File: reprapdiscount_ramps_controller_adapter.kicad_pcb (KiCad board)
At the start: 2 copper layers, 62.1 x 21.2 mm, 0 parts

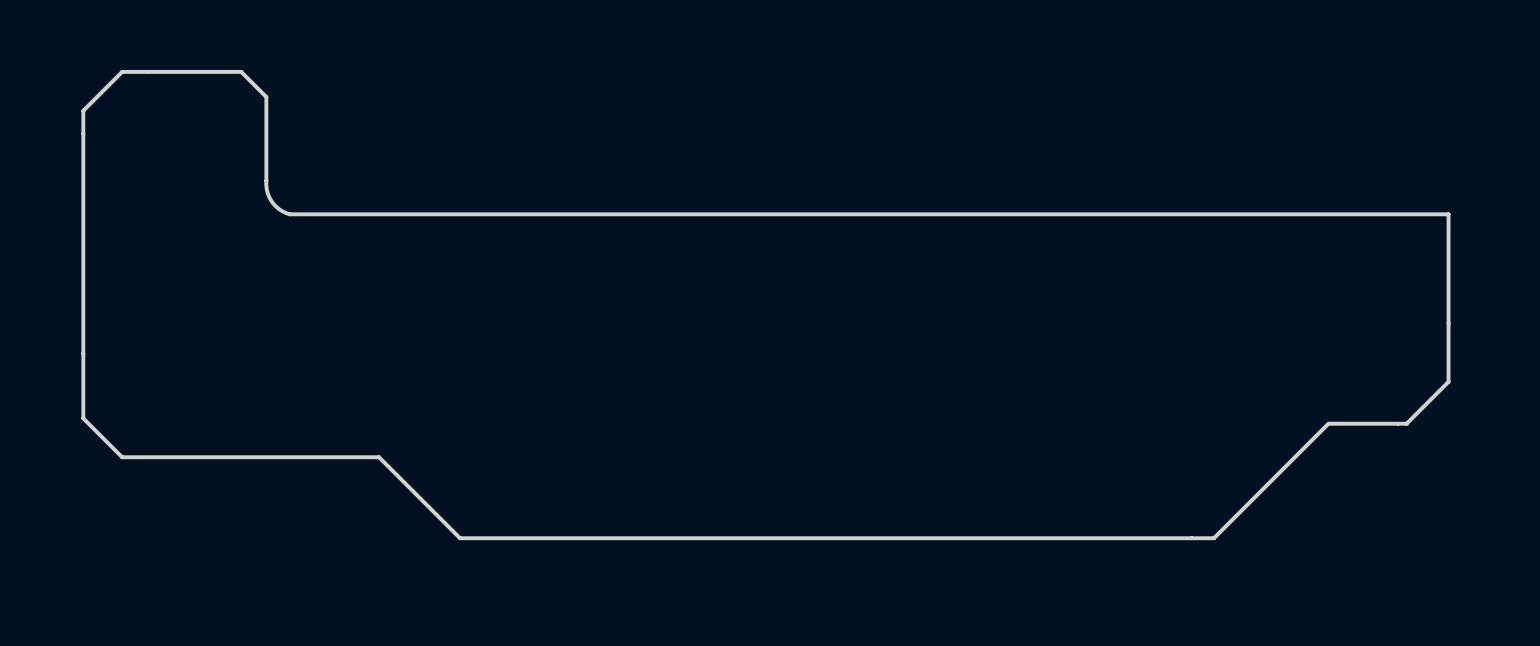
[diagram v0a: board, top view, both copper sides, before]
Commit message: adapter: finish routing
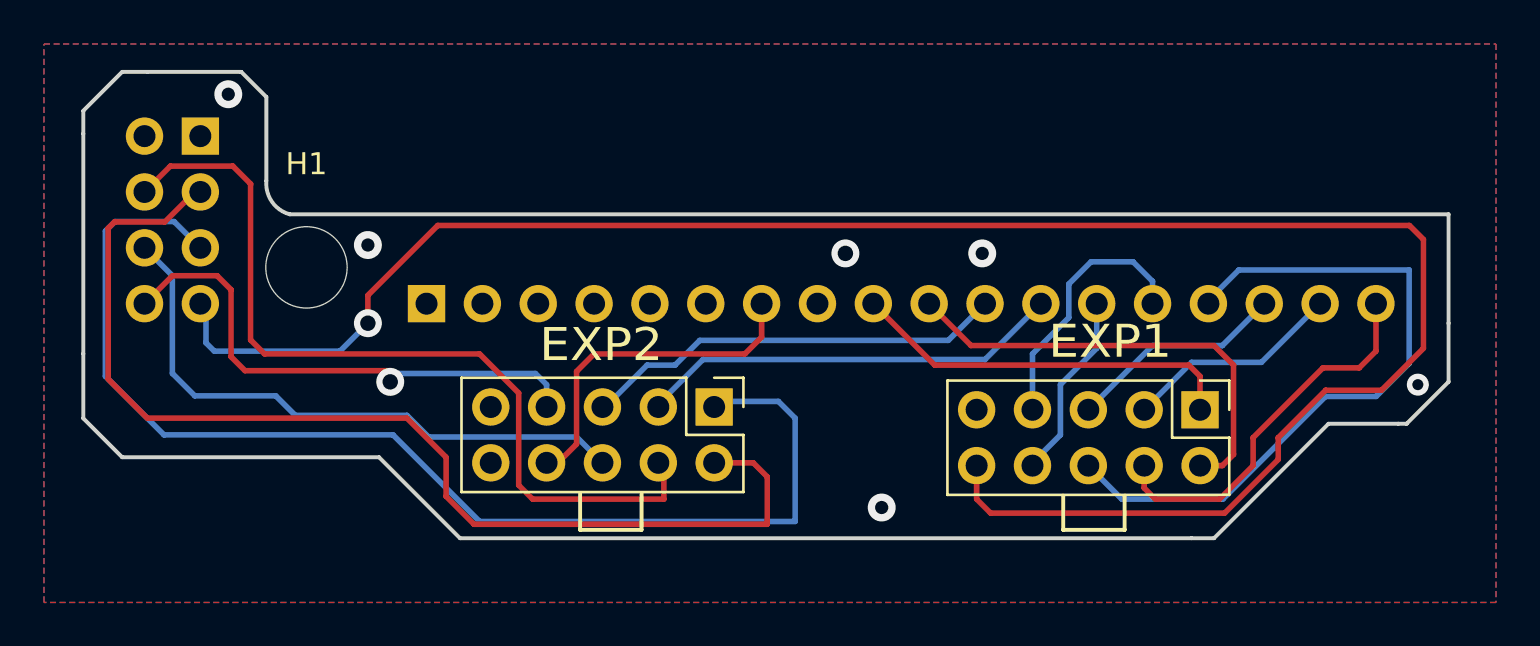
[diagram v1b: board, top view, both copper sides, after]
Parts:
- added AUX-3: Conn_02x04_Odd_Even, Gigahawk:PinSocket_2x04_P2.54mm_Vertical_Flipped, B.Cu at (71.9, -70.7)
- added AUX-4: Conn_01x18, Connector_PinSocket_2.54mm:PinSocket_1x18_P2.54mm_Vertical, B.Cu at (84.7, -63.1)
- added EXP1: Header 5X2, Connector_PinHeader_2.54mm:PinHeader_2x05_P2.54mm_Vertical, F.Cu at (119.9, -58.3)
- added EXP2: Header 5X2, Connector_PinHeader_2.54mm:PinHeader_2x05_P2.54mm_Vertical, F.Cu at (97.8, -58.4)
- added H1: MountingHole, MountingHole:MountingHole_3.7mm, F.Cu at (79.2, -64.8)
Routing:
- net A10: track 0.00 -> 91.5 mm, vias 0 -> 1
- net B1: track 0.00 -> 54.5 mm
- net B2: track 0.00 -> 50.3 mm
- net B4: track 0.00 -> 38.8 mm
- net A6: track 0.00 -> 31.9 mm
- net B6: track 0.00 -> 27.5 mm
- net B7: track 0.00 -> 24.3 mm, vias 0 -> 1
- net A2: track 0.00 -> 20.8 mm
- net B3: track 0.00 -> 19.4 mm
- net B5: track 0.00 -> 19.3 mm
- net A1: track 0.00 -> 17.8 mm
- net A4: track 0.00 -> 17.5 mm
- net B8: track 0.00 -> 15.6 mm
- net A7: track 0.00 -> 12.0 mm
- net A5: track 0.00 -> 10.00 mm
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- added copper zone on B.Cu, net GND
- added copper zone on F.Cu, net GND

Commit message: adapter: update silkscreen
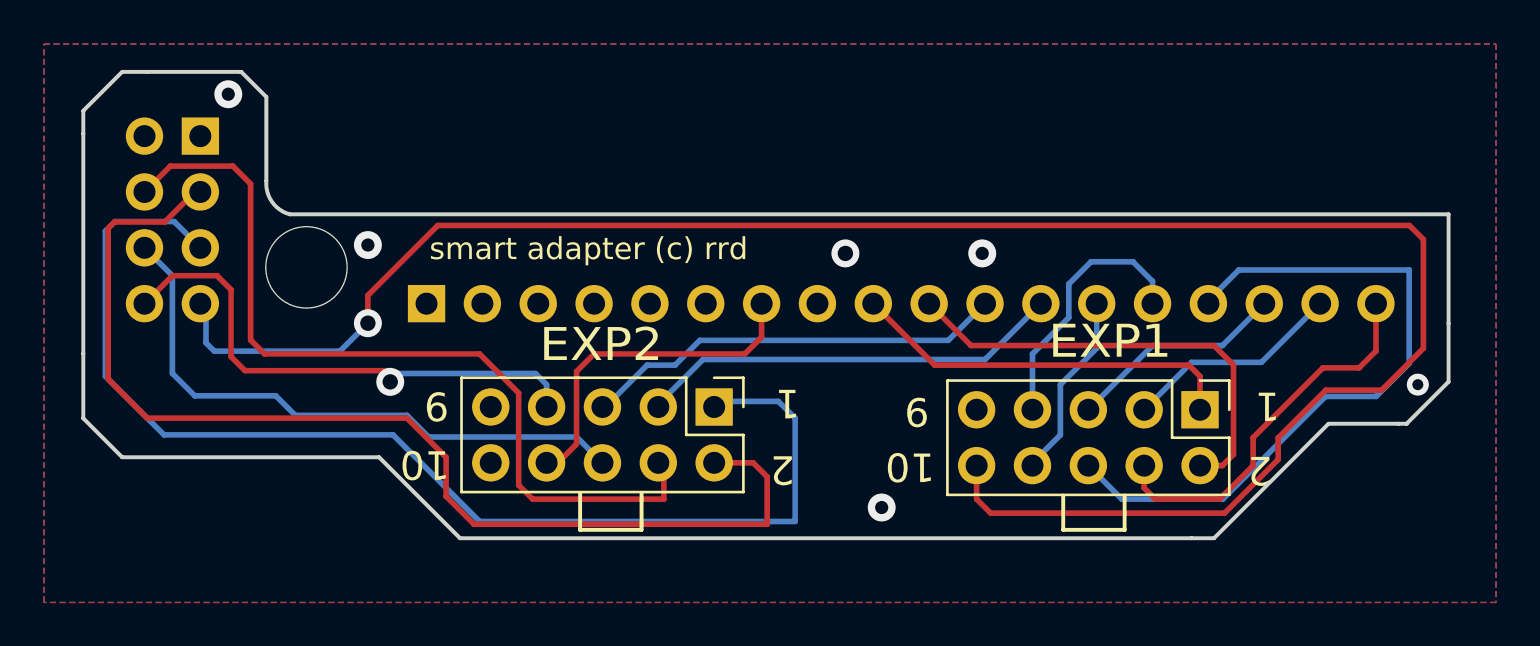
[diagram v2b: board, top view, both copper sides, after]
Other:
- board text added: "1"
- board text added: "10"
- board text added: "2"
- board text added: "9"
- board text added: "smart adapter (c) rrd"
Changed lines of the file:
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@@
     (property "ki_keywords" "mounting hole")
     (attr exclude_from_pos_files)
-    (fp_text reference "H1" (at 0 -4.7) (layer "F.SilkS")
+    (fp_text reference "H1" (at 0 -4.7) (layer "F.SilkS") hide
         (effects (font (size 1 1) (thickness 0.15)))
     )
@@
     (property "ki_keywords" "connector")
     (attr through_hole)
-    (fp_text reference "AUX-3" (at -1.27 2.77) (layer "B.SilkS")
-        (effects (font (size 1 1) (thickness 0.15)) (justify mirror))
+    (fp_text reference "AUX-3" (at -4.5212 -3.2258 270 unlocked) (layer "B.SilkS")
+        (effects (font (size 1.5 1.5) (thickness 0.254) bold) (justify mirror))
     )
     (fp_text value "Conn_02x04_Odd_Even" (at -1.27 -10.39) (layer "B.Fab")
@@
     (property "ki_keywords" "connector")
     (attr through_hole)
-    (fp_text reference "AUX-4" (at 0 2.77 90) (layer "B.SilkS")
-        (effects (font (size 1 1) (thickness 0.15)) (justify mirror))
+    (fp_text reference "AUX-4" (at -2.4638 -38.7858 -180) (layer "B.SilkS")
+        (effects (font (size 1.5 1.5) (thickness 0.254) bold) (justify mirror))
     )
     (fp_text value "Conn_01x18" (at 0 -45.95 90) (layer "B.Fab")
@@
   (gr_line (start 119.507 -52.451) (end 120.523 -52.451)
     (stroke (width 0.1778) (type solid)) (layer "Edge.Cuts"))
+  (gr_text "2" (at 71.8058 -61.1632 90) (layer "B.SilkS")
+    (effects (font (size 1.3 1.3) (thickness 0.2)) (justify mirror))
+  )
+  (gr_text "1" (at 74.3458 -61.214 90) (layer "B.SilkS")
+    (effects (font (size 1.3 1.3) (thickness 0.2)) (justify mirror))
+  )
+  (gr_text "2" (at 100.8888 -55.5752 180) (layer "F.SilkS")
+    (effects (font (size 1.3 1.3) (thickness 0.2)))
+  )
+  (gr_text "1" (at 101.1428 -58.5978 180) (layer "F.SilkS")
+    (effects (font (size 1.3 1.3) (thickness 0.2)))
+  )
+  (gr_text "smart adapter (c) rrd" (at 84.836 -65.024) (layer "F.SilkS")
+    (effects (font (size 1 1) (thickness 0.15)) (justify left bottom))
+  )
+  (gr_text "9" (at 85.1662 -58.4708 180) (layer "F.SilkS")
+    (effects (font (size 1.3 1.3) (thickness 0.2)))
+  )
+  (gr_text "10" (at 84.6328 -55.8038 180) (layer "F.SilkS")
+    (effects (font (size 1.3 1.3) (thickness 0.2)))
+  )
+  (gr_text "2" (at 122.6058 -55.5498 180) (layer "F.SilkS")
+    (effects (font (size 1.3 1.3) (thickness 0.2)))
+  )
+  (gr_text "9" (at 107.0102 -58.2168 180) (layer "F.SilkS")
+    (effects (font (size 1.3 1.3) (thickness 0.2)))
+  )
+  (gr_text "1" (at 122.9614 -58.4708 180) (layer "F.SilkS")
+    (effects (font (size 1.3 1.3) (thickness 0.2)))
+  )
+  (gr_text "10" (at 106.7054 -55.7022 180) (layer "F.SilkS")
+    (effects (font (size 1.3 1.3) (thickness 0.2)))
+  )
   (via (at 129.794 -59.436) (size 1) (drill 0.5) (layers "F.Cu" "B.Cu") (net 0))
   (segment (start 85.598 -56.134) (end 83.82 -57.912) (width 0.254) (layer "F.Cu") (net 2))

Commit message: adapter: clean up schematic
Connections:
- net A1 renamed BEEPER
- net A10 renamed VCC
- net A2 renamed BTN_ENC
- net A3 renamed LCDE
- net A4 renamed LCDRS
- net A5 renamed LCD4
- net A6 renamed LCD5
- net A7 renamed LCD6
- net A8 renamed LCD7
- net B1 renamed SD_MISO
- net B2 renamed HOST_SCK
- net B3 renamed BTN_EN2
- net B4 renamed HOST_CS
- net B5 renamed BTN_EN1
- net B6 renamed HOST_MOSI
- net B7 renamed SD_DET
- net B8 renamed RESET
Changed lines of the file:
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@@
   (net 0 "")
   (net 1 "unconnected-(AUX-3-Pin_2-Pad2)")
-  (net 2 "B2")
-  (net 3 "B4")
-  (net 4 "B1")
-  (net 5 "B6")
-  (net 6 "A10")
-  (net 7 "B7")
+  (net 2 "HOST_SCK")
+  (net 3 "HOST_CS")
+  (net 4 "SD_MISO")
+  (net 5 "HOST_MOSI")
+  (net 6 "VCC")
+  (net 7 "SD_DET")
   (net 8 "unconnected-(AUX-4-Pin_1-Pad1)")
   (net 9 "unconnected-(AUX-4-Pin_2-Pad2)")
@@
   (net 12 "unconnected-(AUX-4-Pin_5-Pad5)")
   (net 13 "unconnected-(AUX-4-Pin_6-Pad6)")
-  (net 14 "B8")
+  (net 14 "RESET")
   (net 15 "unconnected-(AUX-4-Pin_8-Pad8)")
-  (net 16 "A1")
-  (net 17 "A2")
-  (net 18 "B5")
-  (net 19 "B3")
-  (net 20 "A8")
-  (net 21 "A7")
-  (net 22 "A6")
-  (net 23 "A5")
-  (net 24 "A3")
-  (net 25 "A4")
+  (net 16 "BEEPER")
+  (net 17 "BTN_ENC")
+  (net 18 "BTN_EN1")
+  (net 19 "BTN_EN2")
+  (net 20 "LCD7")
+  (net 21 "LCD6")
+  (net 22 "LCD5")
+  (net 23 "LCD4")
+  (net 24 "LCDE")
+  (net 25 "LCDRS")
   (net 26 "B9")
   (net 27 "B10")
@@
       (stroke (width 0.1) (type solid)) (layer "F.Fab"))
     (pad "1" thru_hole rect (at 0 0 270) (size 1.7 1.7) (drill 1) (layers "*.Cu" "*.Mask")
-      (net 4 "B1") (pinfunction "1") (pintype "passive"))
+      (net 4 "SD_MISO") (pinfunction "1") (pintype "passive"))
     (pad "2" thru_hole oval (at 2.54 0 270) (size 1.7 1.7) (drill 1) (layers "*.Cu" "*.Mask")
-      (net 2 "B2") (pinfunction "2") (pintype "passive"))
+      (net 2 "HOST_SCK") (pinfunction "2") (pintype "passive"))
     (pad "3" thru_hole oval (at 0 2.54 270) (size 1.7 1.7) (drill 1) (layers "*.Cu" "*.Mask")
-      (net 19 "B3") (pinfunction "3") (pintype "passive"))
+      (net 19 "BTN_EN2") (pinfunction "3") (pintype "passive"))
     (pad "4" thru_hole oval (at 2.54 2.54 270) (size 1.7 1.7) (drill 1) (layers "*.Cu" "*.Mask")
-      (net 3 "B4") (pinfunction "4") (pintype "passive"))
+      (net 3 "HOST_CS") (pinfunction "4") (pintype "passive"))
     (pad "5" thru_hole oval (at 0 5.08 270) (size 1.7 1.7) (drill 1) (layers "*.Cu" "*.Mask")
-      (net 18 "B5") (pinfunction "5") (pintype "passive"))
+      (net 18 "BTN_EN1") (pinfunction "5") (pintype "passive"))
     (pad "6" thru_hole oval (at 2.54 5.08 270) (size 1.7 1.7) (drill 1) (layers "*.Cu" "*.Mask")
-      (net 5 "B6") (pinfunction "6") (pintype "passive"))
+      (net 5 "HOST_MOSI") (pinfunction "6") (pintype "passive"))
     (pad "7" thru_hole oval (at 0 7.62 270) (size 1.7 1.7) (drill 1) (layers "*.Cu" "*.Mask")
-      (net 7 "B7") (pinfunction "7") (pintype "passive"))
+      (net 7 "SD_DET") (pinfunction "7") (pintype "passive"))
     (pad "8" thru_hole oval (at 2.54 7.62 270) (size 1.7 1.7) (drill 1) (layers "*.Cu" "*.Mask")
-      (net 14 "B8") (pinfunction "8") (pintype "passive"))
+      (net 14 "RESET") (pinfunction "8") (pintype "passive"))
     (pad "9" thru_hole oval (at 0 10.16 270) (size 1.7 1.7) (drill 1) (layers "*.Cu" "*.Mask")
       (net 26 "B9") (pinfunction "9") (pintype "passive"))
@@
       (stroke (width 0.1) (type solid)) (layer "F.Fab"))
     (pad "1" thru_hole rect (at 0 0 270) (size 1.7 1.7) (drill 1) (layers "*.Cu" "*.Mask")
-      (net 16 "A1") (pinfunction "1") (pintype "passive"))
+      (net 16 "BEEPER") (pinfunction "1") (pintype "passive"))
     (pad "2" thru_hole oval (at 2.54 0 270) (size 1.7 1.7) (drill 1) (layers "*.Cu" "*.Mask")
-      (net 17 "A2") (pinfunction "2") (pintype "passive"))
+      (net 17 "BTN_ENC") (pinfunction "2") (pintype "passive"))
     (pad "3" thru_hole oval (at 0 2.54 270) (size 1.7 1.7) (drill 1) (layers "*.Cu" "*.Mask")
-      (net 24 "A3") (pinfunction "3") (pintype "passive"))
+      (net 24 "LCDE") (pinfunction "3") (pintype "passive"))
     (pad "4" thru_hole oval (at 2.54 2.54 270) (size 1.7 1.7) (drill 1) (layers "*.Cu" "*.Mask")
-      (net 25 "A4") (pinfunction "4") (pintype "passive"))
+      (net 25 "LCDRS") (pinfunction "4") (pintype "passive"))
     (pad "5" thru_hole oval (at 0 5.08 270) (size 1.7 1.7) (drill 1) (layers "*.Cu" "*.Mask")
-      (net 23 "A5") (pinfunction "5") (pintype "passive"))
+      (net 23 "LCD4") (pinfunction "5") (pintype "passive"))
     (pad "6" thru_hole oval (at 2.54 5.08 270) (size 1.7 1.7) (drill 1) (layers "*.Cu" "*.Mask")
-      (net 22 "A6") (pinfunction "6") (pintype "passive"))
+      (net 22 "LCD5") (pinfunction "6") (pintype "passive"))
     (pad "7" thru_hole oval (at 0 7.62 270) (size 1.7 1.7) (drill 1) (layers "*.Cu" "*.Mask")
-      (net 21 "A7") (pinfunction "7") (pintype "passive"))
+      (net 21 "LCD6") (pinfunction "7") (pintype "passive"))
     (pad "8" thru_hole oval (at 2.54 7.62 270) (size 1.7 1.7) (drill 1) (layers "*.Cu" "*.Mask")
-      (net 20 "A8") (pinfunction "8") (pintype "passive"))
+      (net 20 "LCD7") (pinfunction "8") (pintype "passive"))
     (pad "9" thru_hole oval (at 0 10.16 270) (size 1.7 1.7) (drill 1) (layers "*.Cu" "*.Mask")
       (net 28 "GND") (pinfunction "9") (pintype "passive"))
     (pad "10" thru_hole oval (at 2.54 10.16 270) (size 1.7 1.7) (drill 1) (layers "*.Cu" "*.Mask")
-      (net 6 "A10") (pinfunction "10") (pintype "passive"))
+      (net 6 "VCC") (pinfunction "10") (pintype "passive"))
     (model "${KICAD6_3DMODEL_DIR}/Connector_PinHeader_2.54mm.3dshapes/PinHeader_2x05_P2.54mm_Vertical.wrl"
       (offset (xyz 0 0 0))
@@
       (net 1 "unconnected-(AUX-3-Pin_2-Pad2)") (pinfunction "Pin_2") (pintype "passive+no_connect"))
     (pad "3" thru_hole oval (at -2.54 -2.54 180) (size 1.7 1.7) (drill 1) (layers "*.Cu" "*.Mask")
-      (net 2 "B2") (pinfunction "Pin_3") (pintype "passive"))
+      (net 2 "HOST_SCK") (pinfunction "Pin_3") (pintype "passive"))
     (pad "4" thru_hole oval (at 0 -2.54 180) (size 1.7 1.7) (drill 1) (layers "*.Cu" "*.Mask")
-      (net 3 "B4") (pinfunction "Pin_4") (pintype "passive"))
+      (net 3 "HOST_CS") (pinfunction "Pin_4") (pintype "passive"))
     (pad "5" thru_hole oval (at -2.54 -5.08 180) (size 1.7 1.7) (drill 1) (layers "*.Cu" "*.Mask")
-      (net 4 "B1") (pinfunction "Pin_5") (pintype "passive"))
+      (net 4 "SD_MISO") (pinfunction "Pin_5") (pintype "passive"))
     (pad "6" thru_hole oval (at 0 -5.08 180) (size 1.7 1.7) (drill 1) (layers "*.Cu" "*.Mask")
-      (net 5 "B6") (pinfunction "Pin_6") (pintype "passive"))
+      (net 5 "HOST_MOSI") (pinfunction "Pin_6") (pintype "passive"))
     (pad "7" thru_hole oval (at -2.54 -7.62 180) (size 1.7 1.7) (drill 1) (layers "*.Cu" "*.Mask")
-      (net 6 "A10") (pinfunction "Pin_7") (pintype "passive"))
+      (net 6 "VCC") (pinfunction "Pin_7") (pintype "passive"))
     (pad "8" thru_hole oval (at 0 -7.62 180) (size 1.7 1.7) (drill 1) (layers "*.Cu" "*.Mask")
-      (net 7 "B7") (pinfunction "Pin_8") (pintype "passive"))
+      (net 7 "SD_DET") (pinfunction "Pin_8") (pintype "passive"))
     (model "${KICAD6_3DMODEL_DIR}/Connector_PinSocket_2.54mm.3dshapes/PinSocket_2x04_P2.54mm_Vertical.wrl"
       (offset (xyz 0 0 0))
@@
       (net 13 "unconnected-(AUX-4-Pin_6-Pad6)") (pinfunction "Pin_6") (pintype "passive+no_connect"))
     (pad "7" thru_hole oval (at 0 -15.24 270) (size 1.7 1.7) (drill 1) (layers "*.Cu" "*.Mask")
-      (net 14 "B8") (pinfunction "Pin_7") (pintype "passive"))
+      (net 14 "RESET") (pinfunction "Pin_7") (pintype "passive"))
     (pad "8" thru_hole oval (at 0 -17.78 270) (size 1.7 1.7) (drill 1) (layers "*.Cu" "*.Mask")
       (net 15 "unconnected-(AUX-4-Pin_8-Pad8)") (pinfunction "Pin_8") (pintype "passive+no_connect"))
     (pad "9" thru_hole oval (at 0 -20.32 270) (size 1.7 1.7) (drill 1) (layers "*.Cu" "*.Mask")
-      (net 16 "A1") (pinfunction "Pin_9") (pintype "passive"))
+      (net 16 "BEEPER") (pinfunction "Pin_9") (pintype "passive"))
     (pad "10" thru_hole oval (at 0 -22.86 270) (size 1.7 1.7) (drill 1) (layers "*.Cu" "*.Mask")
-      (net 17 "A2") (pinfunction "Pin_10") (pintype "passive"))
+      (net 17 "BTN_ENC") (pinfunction "Pin_10") (pintype "passive"))
     (pad "11" thru_hole oval (at 0 -25.4 270) (size 1.7 1.7) (drill 1) (layers "*.Cu" "*.Mask")
-      (net 18 "B5") (pinfunction "Pin_11") (pintype "passive"))
+      (net 18 "BTN_EN1") (pinfunction "Pin_11") (pintype "passive"))
     (pad "12" thru_hole oval (at 0 -27.94 270) (size 1.7 1.7) (drill 1) (layers "*.Cu" "*.Mask")
-      (net 19 "B3") (pinfunction "Pin_12") (pintype "passive"))
+      (net 19 "BTN_EN2") (pinfunction "Pin_12") (pintype "passive"))
     (pad "13" thru_hole oval (at 0 -30.48 270) (size 1.7 1.7) (drill 1) (layers "*.Cu" "*.Mask")
-      (net 20 "A8") (pinfunction "Pin_13") (pintype "passive"))
+      (net 20 "LCD7") (pinfunction "Pin_13") (pintype "passive"))
     (pad "14" thru_hole oval (at 0 -33.02 270) (size 1.7 1.7) (drill 1) (layers "*.Cu" "*.Mask")
-      (net 21 "A7") (pinfunction "Pin_14") (pintype "passive"))
+      (net 21 "LCD6") (pinfunction "Pin_14") (pintype "passive"))
     (pad "15" thru_hole oval (at 0 -35.56 270) (size 1.7 1.7) (drill 1) (layers "*.Cu" "*.Mask")
-      (net 22 "A6") (pinfunction "Pin_15") (pintype "passive"))
+      (net 22 "LCD5") (pinfunction "Pin_15") (pintype "passive"))
     (pad "16" thru_hole oval (at 0 -38.1 270) (size 1.7 1.7) (drill 1) (layers "*.Cu" "*.Mask")
-      (net 23 "A5") (pinfunction "Pin_16") (pintype "passive"))
+      (net 23 "LCD4") (pinfunction "Pin_16") (pintype "passive"))
     (pad "17" thru_hole oval (at 0 -40.64 270) (size 1.7 1.7) (drill 1) (layers "*.Cu" "*.Mask")
-      (net 24 "A3") (pinfunction "Pin_17") (pintype "passive"))
+      (net 24 "LCDE") (pinfunction "Pin_17") (pintype "passive"))
     (pad "18" thru_hole oval (at 0 -43.18 270) (size 1.7 1.7) (drill 1) (layers "*.Cu" "*.Mask")
-      (net 25 "A4") (pinfunction "Pin_18") (pintype "passive"))
+      (net 25 "LCDRS") (pinfunction "Pin_18") (pintype "passive"))
     (model "${KICAD6_3DMODEL_DIR}/Connector_PinSocket_2.54mm.3dshapes/PinSocket_1x18_P2.54mm_Vertical.wrl"
       (offset (xyz 0 0 0))
